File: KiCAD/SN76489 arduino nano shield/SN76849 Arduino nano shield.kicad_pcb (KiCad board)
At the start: 2 copper layers, 70.5 x 62 mm, 17 parts, among them J1 Arduino_sn, J2 audio_debug, J4 I2C, J5 LOGO, J6 gat1, J7 gat2, J8 trs_A-853 geluid uit, U1 PCF8574, U2 LM358, U3 SN76489

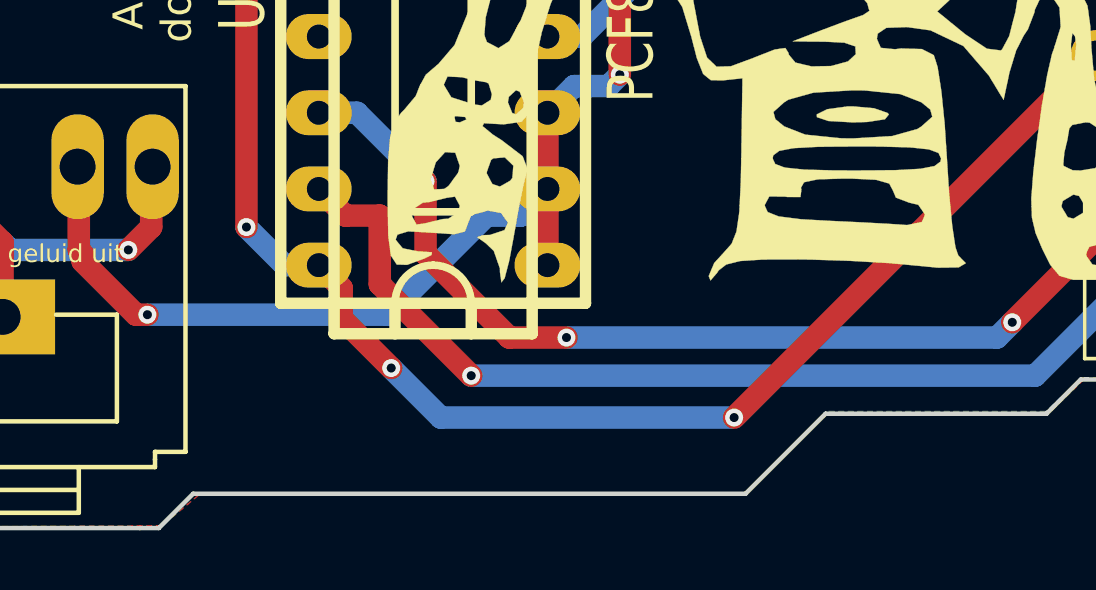
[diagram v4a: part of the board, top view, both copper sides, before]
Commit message: revisie 20180624 0.7.01 naar China
silkscreen toegevoegd
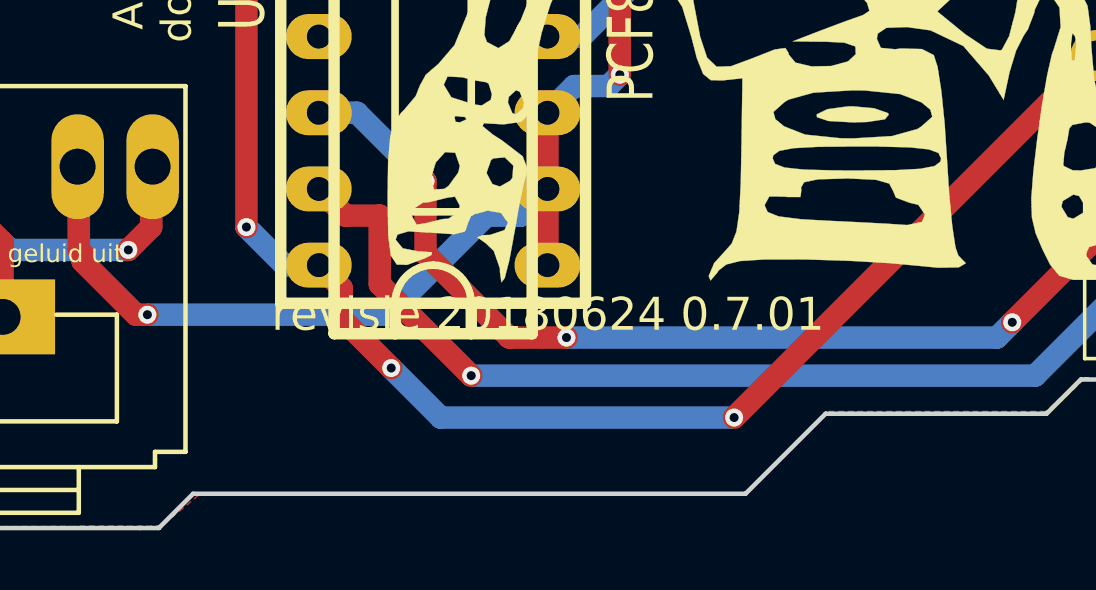
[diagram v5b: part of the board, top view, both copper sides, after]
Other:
- board text added: "revisie 20180624 0.7.01"
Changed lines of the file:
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@@
     (links 40)
     (no_connects 0)
-    (area 101.56402 79.74669 172.922001 141.934001)
+    (area 30.963799 20.067199 101.598801 82.193201)
     (thickness 1.6)
-    (drawings 60)
+    (drawings 61)
     (tracks 374)
     (zones 0)
@@
     (title "EasyLab chiptunes")
     (date 2018-06-24)
-    (rev "revisie 0.7.01")
+    (rev "revisie 20180624 0.7.01")
     (company "©2018 EasyLab4Kids en Michiel Erasmus")
     (comment 3 "versie 20180617 0.7.01")
@@
     )
   )
+  (gr_text "revisie 20180624 0.7.01" (at 59.25 75) (layer F.SilkS)
+    (effects (font (size 1.1 1.1) (thickness 0.275)))
+  )
   (gr_text 220uF (at 72.2376 33.8836) (layer F.SilkS)

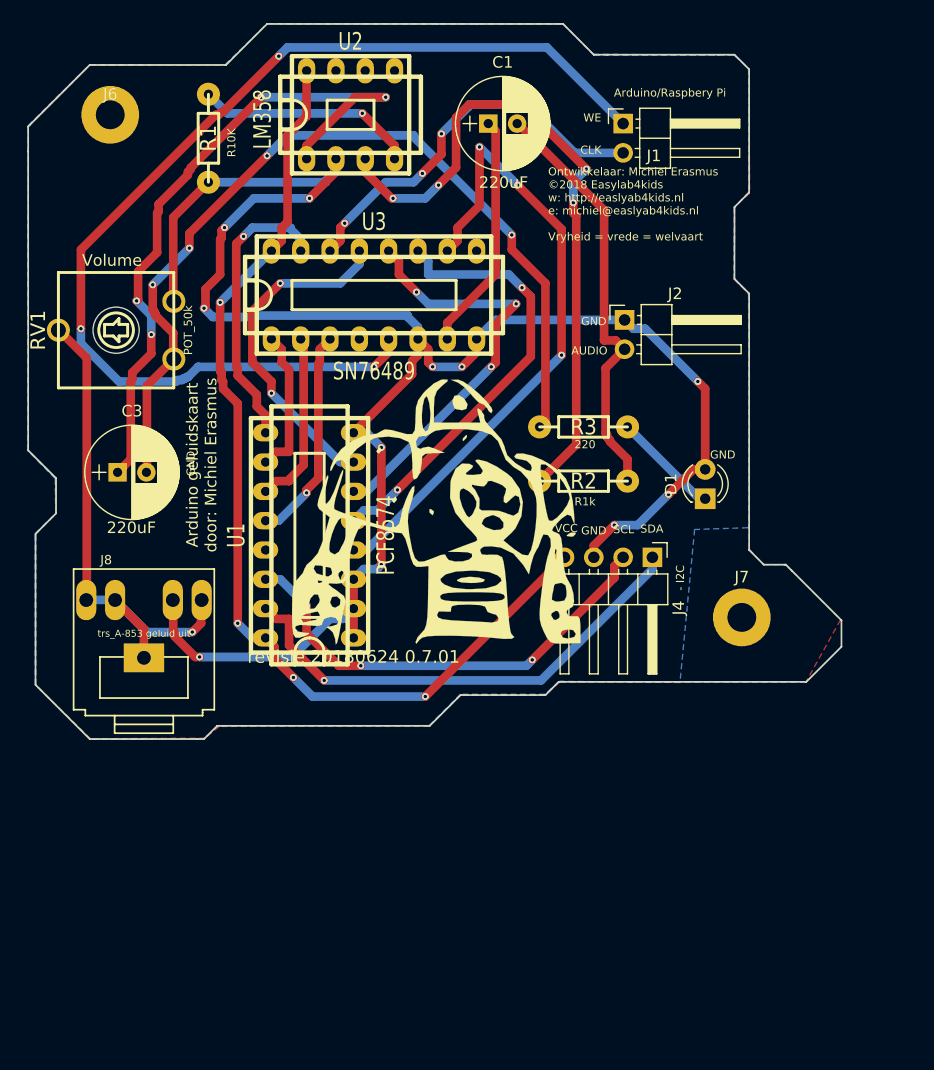
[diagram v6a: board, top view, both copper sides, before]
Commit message: 20180719 0.7.03 OLED
Groot bugfix;

POTmeter verbinding
LM358 nu dual op
PWM pin is verbonde met LM358 out2
Geluidsuitgang debug in stereo
OLED skerm I2c toegevoegd.
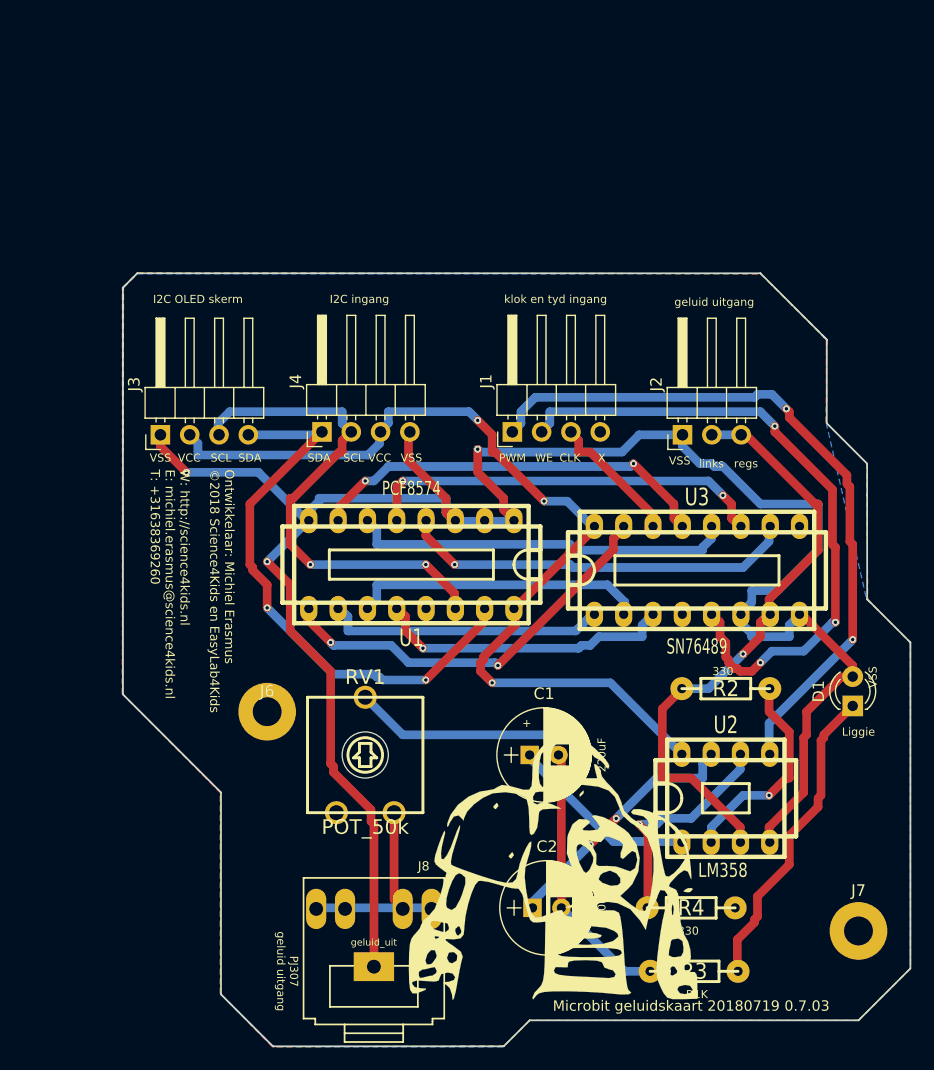
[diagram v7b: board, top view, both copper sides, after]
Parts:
- removed C3: CP_220uF, Capacitors_THT:CP_Radial_D8.0mm_P2.50mm
- removed R1: R10k, w_pth_resistors:RC03
- added C2: CP_220uF, Capacitors_THT:CP_Radial_D8.0mm_P2.50mm, F.Cu at (74.8, 96.8)
- added J3: OLED_wit, Pin_Headers:Pin_Header_Angled_1x04_Pitch2.54mm, F.Cu at (42.5, 55.8)
- added R4: 330, w_pth_resistors:RC03, F.Cu at (88.5, 96.8)
- J1: value Arduino_sn -> Arduino_in; footprint Pin_Headers:Pin_Header_Angled_1x02_Pitch2.54mm -> Pin_Headers:Pin_Header_Angled_1x04_Pitch2.54mm
- J2: footprint Pin_Headers:Pin_Header_Angled_1x02_Pitch2.54mm -> Pin_Headers:Pin_Header_Angled_1x03_Pitch2.54mm
- J4: value I2C -> I2C_in
- J8: value trs_A-853 geluid uit -> geluid_uit
- R2: value R1k -> 330
- R3: value 220 -> R1k
- moved U2 67.6 mm to (91.5, 87.2)
- moved C1 54.8 mm to (74.5, 83.5)
- moved J6 53.5 mm to (51.8, 79.8)
- moved R3 48.1 mm to (88.8, 102.2)
- moved RV1 42.7 mm to (60.2, 83.5), turned to 180 degrees
- moved U3 36.8 mm to (89.0, 67.5)
- moved J8 33.4 mm to (61.0, 100.2)
- moved J5 32.4 mm to (76.6, 93.0)
- moved J4 30.6 mm to (56.5, 55.5), turned to 90 degrees
- moved J7 29.0 mm to (103.0, 98.8)
- moved J1 28.4 mm to (73.0, 55.5), turned to 90 degrees
- moved D1 22.0 mm to (102.5, 79.2)
- moved R2 21.8 mm to (91.5, 77.8), turned to 180 degrees
- moved J2 11.1 mm to (87.8, 55.8), turned to 90 degrees
- moved U1 9.18 mm to (64.2, 67.0), turned to 180 degrees
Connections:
- C1 pad 1: /Audio -> Net-(C1-Pad1)
- J1 pad 1: /WE -> /PWM
- J1 pad 2: /Clock -> /WE
- J2 pad 2: Net-(C1-Pad2) -> /Audio
- J4 pad 3: GND -> /VCC
- J4 pad 4: /VCC -> GND
- J8 pad 1: Net-(J8-Pad1) -> GND
- J8 pad 2: Net-(J8-Pad1) -> Net-(J8-Pad2)
- J8 pad 3: Net-(J8-Pad1) -> Net-(J8-Pad2)
- J8 pad 4: Net-(J8-Pad1) -> Net-(J8-Pad2)
- J8 pad 5: GND -> Net-(J8-Pad2)
- R2 pad 2: Net-(C1-Pad2) -> /Audio
- R3 pad 2: Net-(C3-Pad2) -> Net-(C1-Pad2)
- RV1 pad 1: Net-(C3-Pad2) -> (no net)
- RV1 pad 2: Net-(J8-Pad1) -> Net-(C1-Pad2)
- RV1 pad 3: GND -> Net-(J8-Pad2)
- U2 pad 1: Net-(C3-Pad1) -> Net-(C1-Pad1)
- U2 pad 2: GND -> Net-(R2-Pad1)
- U2 pad 3: Net-(R2-Pad1) -> /Audio
- U2 pad 4: Net-(R1-Pad2) -> GND
- U2 pad 5: (no net) -> /PWM
- U2 pad 6: (no net) -> Net-(R4-Pad1)
- U2 pad 7: (no net) -> Net-(C2-Pad1)
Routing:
- net Net-(C3-Pad2): track 77.0 -> 0.00 mm, vias 4 -> 0
- net /PWM: track 0.00 -> 61.7 mm, vias 0 -> 2
- net Net-(C3-Pad1): track 59.3 -> 0.00 mm, vias 4 -> 0
- net Net-(J8-Pad1): track 44.2 -> 0.00 mm, vias 1 -> 0
- net Net-(R2-Pad1): track 58.6 -> 18.4 mm, vias 4 -> 1
- net /WE: track 95.3 -> 57.5 mm
- net /Audio: track 20.7 -> 52.5 mm, vias 0 -> 1
- net /Clock: track 34.2 -> 12.0 mm, vias 3 -> 0
- net Net-(C2-Pad1): track 0.00 -> 22.1 mm, vias 0 -> 2
- net /P0: track 56.2 -> 34.5 mm, vias 3 -> 1
- net Net-(R4-Pad1): track 0.00 -> 19.7 mm, vias 0 -> 1
- net Net-(J8-Pad2): track 0.00 -> 19.2 mm
- net Net-(R1-Pad2): track 19.1 -> 0.00 mm, vias 1 -> 0
- net Net-(D1-Pad1): track 9.31 -> 27.2 mm
- net Net-(C1-Pad1): track 0.00 -> 16.6 mm
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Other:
- board size 70.5 x 62 mm -> 68.2 x 67 mm
- board text added: "+"
- board text added: "330"
- board text added: "I2C OLED skerm"
- board text added: "I2C ingang"
- board text added: "Liggie"
- board text added: "Microbit geluidskaart 20180719 0.7.03"
- board text added: "Nooit hoef jou kinders wat trou is te vra: Wat beteken jou vlag dan, Suid-Afrika? Ons weet hy’s die seël van ons vryheid en reg Vir naaste en vreemde, vir oorman en kneg; Die pand van ons erfnis, geslag op geslag, Om te hou vir ons kinders se kinders wat wag; Ons nasie se grondbrief van eiendomsland, Uitgegee op gesag van die Hoogste se hand. Oor ons hoof sal ons hys, in ons hart sal ons dra, Die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"
- board text added: "Ontwikkelaar: Michiel Erasmus ©2018 Science4Kids en EasyLab4Kids W: http://science4kids.nl E: michiel.erasmus@science4kids.nl T: +31638369260"
- board text added: "PJ307 geluid uitgang"
- board text added: "PWM"
- board text added: "R1K"
- board text added: "VSS"
- board text added: "X"
- board text added: "geluid uitgang"
- board text added: "klok en tyd ingang"
- board text added: "links"
- board text added: "regs"
- board text removed: "- I2C"
- board text removed: "220"
- board text removed: "AUDIO"
- board text removed: "Arduino geluidskaart door: Michiel Erasmus"
- board text removed: "Arduino/Raspbery Pi"
- board text removed: "GND"
- board text removed: "Ontwikkelaar: Michiel Erasmus ©2018 Easylab4kids w: http://easlyab4kids.nl e: michiel@easlyab4kids.nl Vryheid = vrede = welvaart"
- board text removed: "R10K"
- board text removed: "R1k"
- board text removed: "Volume"
- board text removed: "revisie 20180624 0.7.01"

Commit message: update
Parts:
- removed J5: LOGO, lib_michiel:Sovjet_simpits_logo01
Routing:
- removed copper zone on B.Cu, net (none)
- removed copper zone on F.Cu, net (none)
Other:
- board text removed: "Nooit hoef jou kinders wat trou is te vra: Wat beteken jou vlag dan, Suid-Afrika? Ons weet hy’s die seël van ons vryheid en reg Vir naaste en vreemde, vir oorman en kneg; Die pand van ons erfnis, geslag op geslag, Om te hou vir ons kinders se kinders wat wag; Ons nasie se grondbrief van eiendomsland, Uitgegee op gesag van die Hoogste se hand. Oor ons hoof sal ons hys, in ons hart sal ons dra, Die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"
